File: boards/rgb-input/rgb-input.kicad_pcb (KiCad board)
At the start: 2 copper layers, 184.5 x 137 mm, 181 parts, among them J1 Conn_01x02, J13 I2C, J14 Conn_01x04, J2 Conn_01x02, J20 Conn_01x04, J21 Conn_01x02, J22 Conn_01x02, J23 Conn_01x02, J24 Conn_01x02, J25 Conn_01x02, J26 Conn_01x04, J27 Conn_01x04, J28 Conn_01x02, J29 Conn_01x02, J3 Conn_01x02, J30 Conn_01x04, J31 Conn_01x04, J32 Conn_01x04, J33 Conn_01x04, J34 Conn_01x04, J35 Conn_01x04, J36 Conn_01x04, J37 Conn_01x04, J38 Conn_01x04, J39 Conn_01x04, J4 Conn_01x02, J40 Conn_01x04, J41 Conn_01x04, J5 Conn_01x02, J6 Conn_01x02, J7 Conn_01x02, J8 Conn_01x02, J9 Conn_01x02, U1 ESP32-DEVKITC, U13 MCP1502, U15 MCP3425A0T-ECH, U2 MCP3208, U3 R-78K5.0-1.0, U5 TLC5947DAP, U6 TLC5947DAP

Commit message: figured out most of the components, working on placement
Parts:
- removed J1, J2, J21, J22, J23, J24, J25, J28, J29, J3, J4, J5, J6, J7, J8, J9: Conn_01x02, Connector_JST:JST_PH_B2B-PH-K_1x02_P2.00mm_Vertical
- removed J14, J20, J26, J27, J30, J31, J32, J33, J34, J35, J36, J37, J38, J39, J40, J41: Conn_01x04, Connector_JST:JST_PH_B4B-PH-K_1x04_P2.00mm_Vertical
- added ADC0: ~, Connector_JST:JST_PH_B3B-PH-K_1x03_P2.00mm_Vertical, F.Cu at (63.2, 18.2)
- added ADC1: ~, Connector_JST:JST_PH_B3B-PH-K_1x03_P2.00mm_Vertical, F.Cu at (63.2, 25.3)
- added ADC2: ~, Connector_JST:JST_PH_B3B-PH-K_1x03_P2.00mm_Vertical, F.Cu at (63.2, 32.9)
- added ADC3: ~, Connector_JST:JST_PH_B3B-PH-K_1x03_P2.00mm_Vertical, F.Cu at (63.2, 40.5)
- added ADC4: ~, Connector_JST:JST_PH_B3B-PH-K_1x03_P2.00mm_Vertical, F.Cu at (63.2, 48.1)
- added ADC5: ~, Connector_JST:JST_PH_B3B-PH-K_1x03_P2.00mm_Vertical, F.Cu at (63.2, 55.7)
- added ADC6: ~, Connector_JST:JST_PH_B3B-PH-K_1x03_P2.00mm_Vertical, F.Cu at (63.2, 63.4)
- added ADC7: ~, Connector_JST:JST_PH_B3B-PH-K_1x03_P2.00mm_Vertical, F.Cu at (63.2, 71.0)
- added INPUT0: ~, Connector_JST:JST_PH_B2B-PH-K_1x02_P2.00mm_Vertical, F.Cu at (133.8, 18.2)
- added INPUT1: ~, Connector_JST:JST_PH_B2B-PH-K_1x02_P2.00mm_Vertical, F.Cu at (133.8, 25.8)
- added INPUT10: ~, Connector_JST:JST_PH_B2B-PH-K_1x02_P2.00mm_Vertical, F.Cu at (133.8, 94.4)
- added INPUT11: ~, Connector_JST:JST_PH_B2B-PH-K_1x02_P2.00mm_Vertical, F.Cu at (133.8, 102.0)
- added INPUT12: ~, Connector_JST:JST_PH_B2B-PH-K_1x02_P2.00mm_Vertical, F.Cu at (133.8, 109.6)
- added INPUT13: ~, Connector_JST:JST_PH_B2B-PH-K_1x02_P2.00mm_Vertical, F.Cu at (133.8, 117.2)
- added INPUT14: ~, Connector_JST:JST_PH_B2B-PH-K_1x02_P2.00mm_Vertical, F.Cu at (133.8, 124.9)
- added INPUT15: ~, Connector_JST:JST_PH_B2B-PH-K_1x02_P2.00mm_Vertical, F.Cu at (133.8, 132.5)
- added INPUT2: ~, Connector_JST:JST_PH_B2B-PH-K_1x02_P2.00mm_Vertical, F.Cu at (133.8, 33.4)
- added INPUT3: ~, Connector_JST:JST_PH_B2B-PH-K_1x02_P2.00mm_Vertical, F.Cu at (133.8, 41.0)
- added INPUT4: ~, Connector_JST:JST_PH_B2B-PH-K_1x02_P2.00mm_Vertical, F.Cu at (133.8, 48.7)
- added INPUT5: ~, Connector_JST:JST_PH_B2B-PH-K_1x02_P2.00mm_Vertical, F.Cu at (133.8, 56.3)
- added INPUT6: ~, Connector_JST:JST_PH_B2B-PH-K_1x02_P2.00mm_Vertical, F.Cu at (133.8, 63.9)
- added INPUT7: ~, Connector_JST:JST_PH_B2B-PH-K_1x02_P2.00mm_Vertical, F.Cu at (133.8, 71.5)
- added INPUT8: ~, Connector_JST:JST_PH_B2B-PH-K_1x02_P2.00mm_Vertical, F.Cu at (133.8, 79.1)
- added INPUT9: ~, Connector_JST:JST_PH_B2B-PH-K_1x02_P2.00mm_Vertical, F.Cu at (133.8, 86.8)
- added J42: INPUTS, Connector_IDC:IDC-Header_2x10_P2.54mm_Vertical, F.Cu at (4.77, 100.7)
- added J46: RGB, Connector_IDC:IDC-Header_2x25_P2.54mm_Vertical, F.Cu at (177.7, 105.8)
- added RGB0: ~, Connector_JST:JST_PH_B4B-PH-K_1x04_P2.00mm_Vertical, F.Cu at (151.6, 18.2)
- added RGB1: ~, Connector_JST:JST_PH_B4B-PH-K_1x04_P2.00mm_Vertical, F.Cu at (151.6, 25.8)
- added RGB10: ~, Connector_JST:JST_PH_B4B-PH-K_1x04_P2.00mm_Vertical, F.Cu at (151.6, 94.4)
- added RGB11: ~, Connector_JST:JST_PH_B4B-PH-K_1x04_P2.00mm_Vertical, F.Cu at (151.6, 102.0)
- added RGB12: ~, Connector_JST:JST_PH_B4B-PH-K_1x04_P2.00mm_Vertical, F.Cu at (151.6, 109.6)
- added RGB13: ~, Connector_JST:JST_PH_B4B-PH-K_1x04_P2.00mm_Vertical, F.Cu at (151.6, 117.2)
- added RGB14: ~, Connector_JST:JST_PH_B4B-PH-K_1x04_P2.00mm_Vertical, F.Cu at (151.6, 124.9)
- added RGB15: ~, Connector_JST:JST_PH_B4B-PH-K_1x04_P2.00mm_Vertical, F.Cu at (151.6, 132.5)
- added RGB2: ~, Connector_JST:JST_PH_B4B-PH-K_1x04_P2.00mm_Vertical, F.Cu at (151.6, 33.4)
- added RGB3: ~, Connector_JST:JST_PH_B4B-PH-K_1x04_P2.00mm_Vertical, F.Cu at (151.6, 41.0)
- added RGB4: ~, Connector_JST:JST_PH_B4B-PH-K_1x04_P2.00mm_Vertical, F.Cu at (151.6, 48.7)
- added RGB5: ~, Connector_JST:JST_PH_B4B-PH-K_1x04_P2.00mm_Vertical, F.Cu at (151.6, 56.3)
- added RGB6: ~, Connector_JST:JST_PH_B4B-PH-K_1x04_P2.00mm_Vertical, F.Cu at (151.6, 63.9)
- added RGB7: ~, Connector_JST:JST_PH_B4B-PH-K_1x04_P2.00mm_Vertical, F.Cu at (151.6, 71.5)
- added RGB8: ~, Connector_JST:JST_PH_B4B-PH-K_1x04_P2.00mm_Vertical, F.Cu at (151.6, 79.1)
- added RGB9: ~, Connector_JST:JST_PH_B4B-PH-K_1x04_P2.00mm_Vertical, F.Cu at (151.6, 86.8)
- moved U6 217.7 mm to (175.7, 122.3)
- moved U5 206.8 mm to (177.0, 28.3)
- moved H2 185.9 mm to (180.8, 133.8)
- moved C3 107.2 mm to (125.8, 185.9)
- moved D2 107.2 mm to (125.8, 188.4)
- moved R1 107.2 mm to (122.0, 188.4)
- moved R2 107.2 mm to (122.0, 185.9)
- moved C17 81.4 mm to (115.1, 168.1)
- moved D12 81.4 mm to (111.8, 194.8)
- moved D13 81.4 mm to (100.9, 194.8)
- moved R22 81.4 mm to (116.0, 179.6)
- moved R25 81.4 mm to (126.9, 179.6)
- moved R26 81.4 mm to (105.2, 179.6)
- moved R4 81.4 mm to (94.3, 178.1)
- moved R44 81.4 mm to (79.9, 178.1)
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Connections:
- net /ADC Input/INPUT renamed /ADC Input0/INPUT
- net /Input Switch0/INPUT renamed /INPUT0
- net /Input Switch1/INPUT renamed /INPUT1
- net /Input Switch10/INPUT renamed /INPUT10
- net /Input Switch11/INPUT renamed /INPUT11
- net /Input Switch12/INPUT renamed /INPUT12
- net /Input Switch13/INPUT renamed /INPUT13
- net /Input Switch14/INPUT renamed /INPUT14
- net /Input Switch15/INPUT renamed /INPUT15
- net /Input Switch2/INPUT renamed /INPUT2
- net /Input Switch3/INPUT renamed /INPUT3
- net /Input Switch4/INPUT renamed /INPUT4
- net /Input Switch5/INPUT renamed /INPUT5
- net /Input Switch6/INPUT renamed /INPUT6
- net /Input Switch7/INPUT renamed /INPUT7
- net /Input Switch8/INPUT renamed /INPUT8
- net /Input Switch9/INPUT renamed /INPUT9
- U5 pad 10: /LEDS/LED Driver1/OUT5 -> /LEDS/BLUE9
- U5 pad 11: /LEDS/LED Driver1/OUT6 -> /LEDS/RED10
- U5 pad 12: /LEDS/LED Driver1/OUT7 -> /LEDS/GREEN10
- U5 pad 13: /LEDS/LED Driver1/OUT8 -> /LEDS/BLUE10
- U5 pad 14: /LEDS/LED Driver1/OUT9 -> /LEDS/RED11
- U5 pad 15: /LEDS/LED Driver1/OUT10 -> /LEDS/GREEN11
- U5 pad 16: /LEDS/LED Driver1/OUT11 -> /LEDS/BLUE11
- U5 pad 17: /LEDS/LED Driver1/OUT12 -> /LEDS/RED12
- U5 pad 18: /LEDS/LED Driver1/OUT13 -> /LEDS/GREEN12
- U5 pad 19: /LEDS/LED Driver1/OUT14 -> /LEDS/BLUE12
- U5 pad 20: /LEDS/LED Driver1/OUT15 -> /LEDS/RED13
- U5 pad 21: /LEDS/LED Driver1/OUT16 -> /LEDS/GREEN13
- U5 pad 22: /LEDS/LED Driver1/OUT17 -> /LEDS/BLUE13
- U5 pad 23: /LEDS/LED Driver1/OUT18 -> /LEDS/RED14
- U5 pad 24: /LEDS/LED Driver1/OUT19 -> /LEDS/GREEN14
- U5 pad 25: /LEDS/LED Driver1/OUT20 -> /LEDS/BLUE14
- U5 pad 26: /LEDS/LED Driver1/OUT21 -> /LEDS/RED15
- U5 pad 27: /LEDS/LED Driver1/OUT22 -> /LEDS/GREEN15
- U5 pad 28: /LEDS/LED Driver1/OUT23 -> /LEDS/BLUE15
- U5 pad 5: /LEDS/LED Driver1/OUT0 -> /LEDS/RED8
- U5 pad 6: /LEDS/LED Driver1/OUT1 -> /LEDS/GREEN8
- U5 pad 7: /LEDS/LED Driver1/OUT2 -> /LEDS/BLUE8
- U5 pad 8: /LEDS/LED Driver1/OUT3 -> /LEDS/RED9
- U5 pad 9: /LEDS/LED Driver1/OUT4 -> /LEDS/GREEN9
- U6 pad 10: /LEDS/LED Driver/OUT5 -> /LEDS/BLUE1
- U6 pad 11: /LEDS/LED Driver/OUT6 -> /LEDS/RED2
- U6 pad 12: /LEDS/LED Driver/OUT7 -> /LEDS/GREEN2
- U6 pad 13: /LEDS/LED Driver/OUT8 -> /LEDS/BLUE2
- U6 pad 14: /LEDS/LED Driver/OUT9 -> /LEDS/RED3
- U6 pad 15: /LEDS/LED Driver/OUT10 -> /LEDS/GREEN3
- U6 pad 16: /LEDS/LED Driver/OUT11 -> /LEDS/BLUE3
- U6 pad 17: /LEDS/LED Driver/OUT12 -> /LEDS/RED4
- U6 pad 18: /LEDS/LED Driver/OUT13 -> /LEDS/GREEN4
- U6 pad 19: /LEDS/LED Driver/OUT14 -> /LEDS/BLUE4
- U6 pad 20: /LEDS/LED Driver/OUT15 -> /LEDS/RED5
- U6 pad 21: /LEDS/LED Driver/OUT16 -> /LEDS/GREEN5
- U6 pad 22: /LEDS/LED Driver/OUT17 -> /LEDS/BLUE5
- U6 pad 23: /LEDS/LED Driver/OUT18 -> /LEDS/RED6
- U6 pad 24: /LEDS/LED Driver/OUT19 -> /LEDS/GREEN6
- U6 pad 25: /LEDS/LED Driver/OUT20 -> /LEDS/BLUE6
- U6 pad 26: /LEDS/LED Driver/OUT21 -> /LEDS/RED7
- U6 pad 27: /LEDS/LED Driver/OUT22 -> /LEDS/GREEN7
- U6 pad 28: /LEDS/LED Driver/OUT23 -> /LEDS/BLUE7
- U6 pad 5: /LEDS/LED Driver/OUT0 -> /LEDS/RED0
- U6 pad 6: /LEDS/LED Driver/OUT1 -> /LEDS/GREEN0
- U6 pad 7: /LEDS/LED Driver/OUT2 -> /LEDS/BLUE0
- U6 pad 8: /LEDS/LED Driver/OUT3 -> /LEDS/RED1
- U6 pad 9: /LEDS/LED Driver/OUT4 -> /LEDS/GREEN1
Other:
- outline, holes or cut-outs redrawn
- board text removed: "CAN"
- board text removed: "LFAN"
- board text removed: "RFAN"
- board text removed: "RX"
- board text removed: "TX"

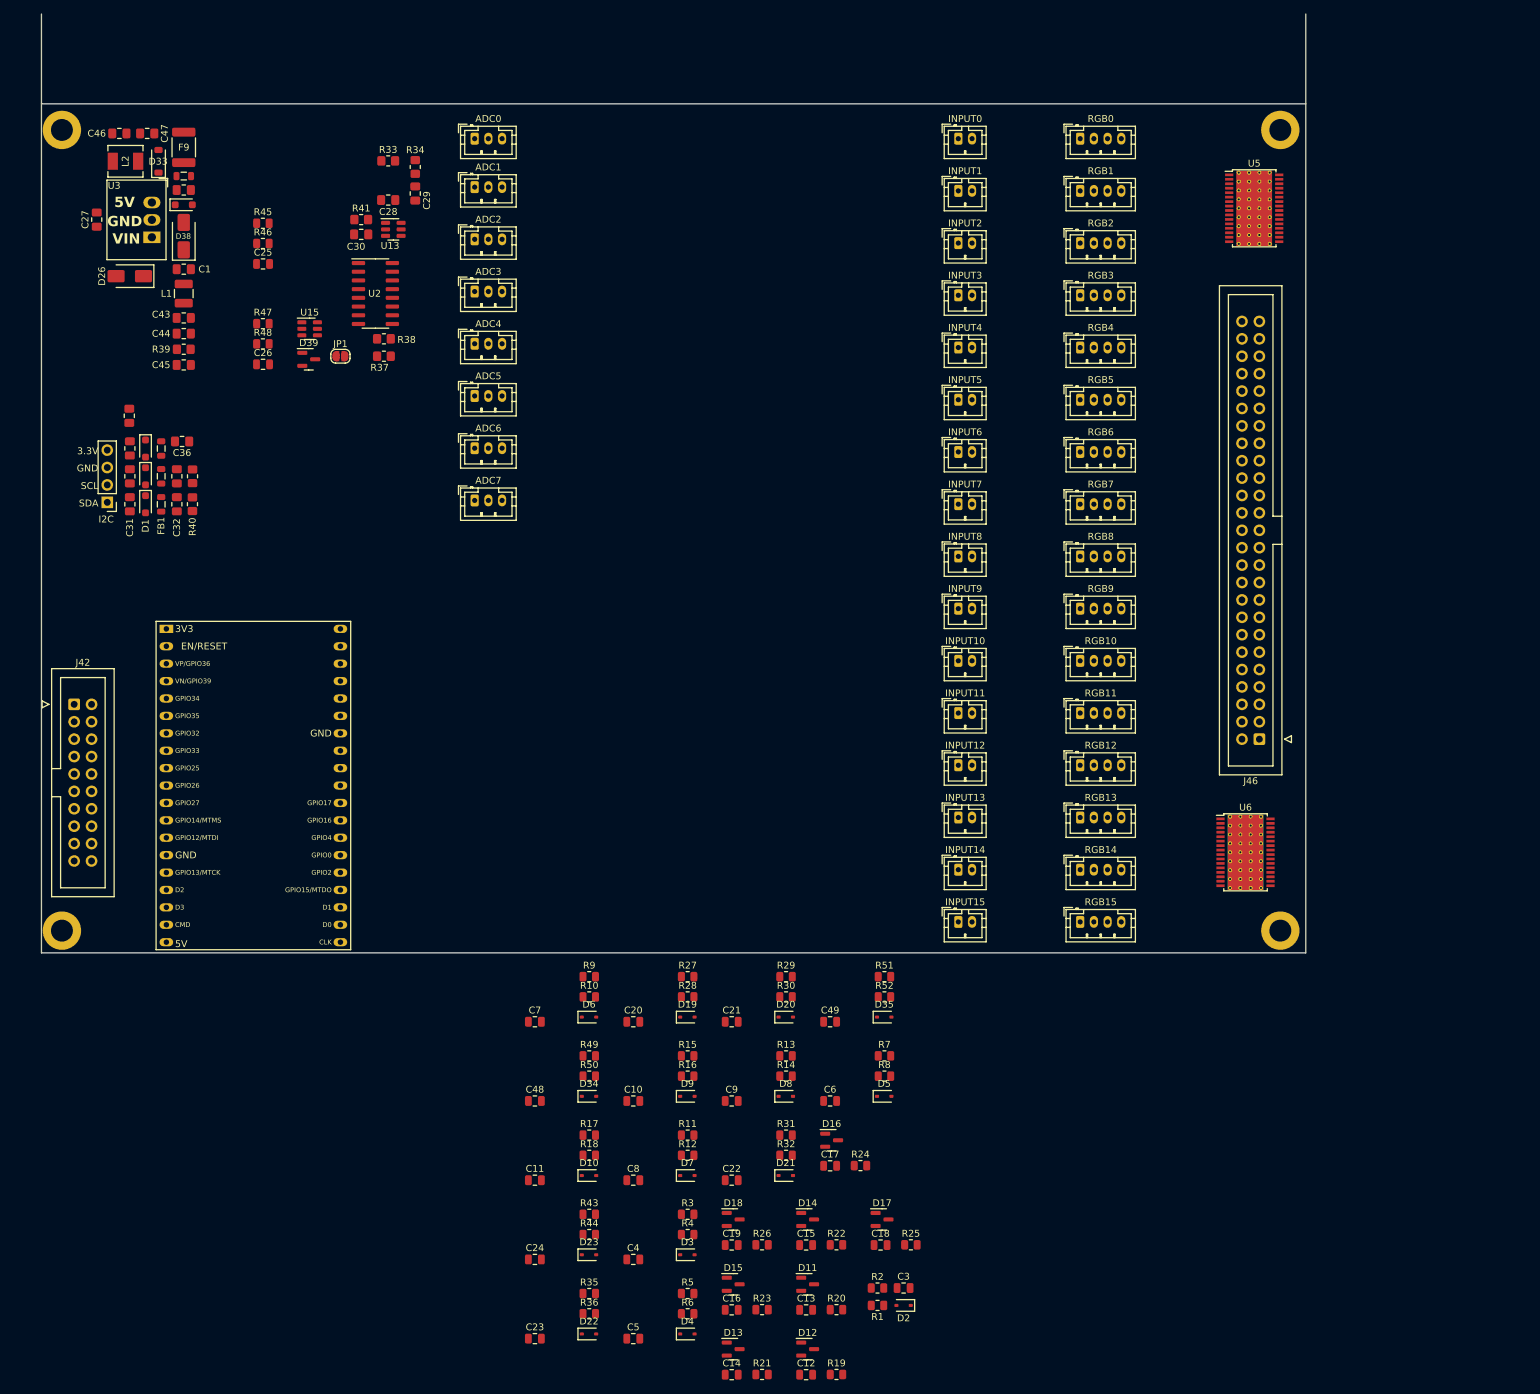
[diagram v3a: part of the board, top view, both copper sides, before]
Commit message: more layout checks on the input board
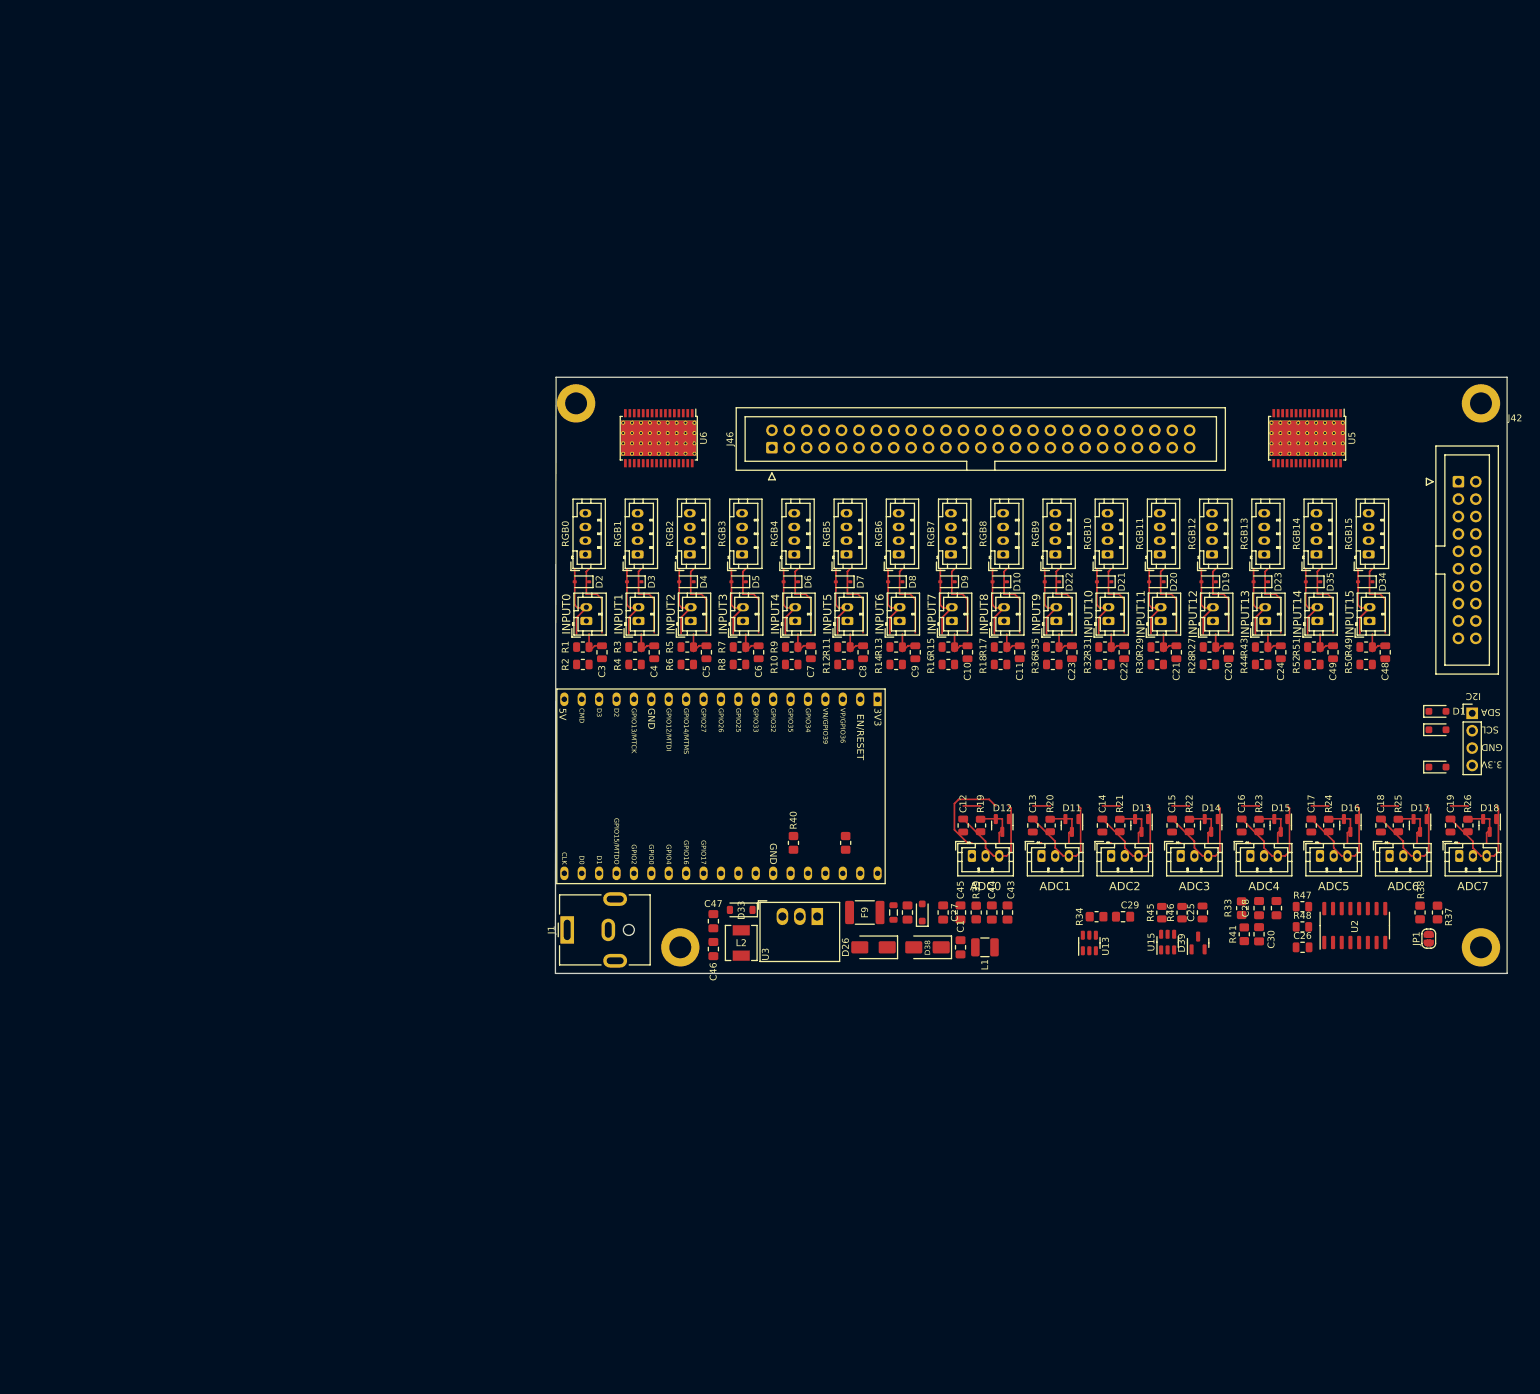
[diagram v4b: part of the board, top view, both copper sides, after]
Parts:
- removed C31, C32, C33, C34: 33pF, Capacitor_SMD:C_0805_2012Metric_Pad1.18x1.45mm_HandSolder
- removed C35, C36: 10uF, Capacitor_SMD:C_0805_2012Metric_Pad1.18x1.45mm_HandSolder
- removed FB1, FB2, FB3: GZ2012D601TF, Inductor_SMD:L_0805_2012Metric
- added J1: Barrel_Jack, Connector_BarrelJack:BarrelJack_CUI_PJ-063AH_Horizontal, F.Cu at (76.7, 133.7)
- moved J42 204.6 mm to (206.8, 68.2)
- moved J13 201.6 mm to (208.8, 102.0), turned to 0 degrees
- moved D28 194.2 mm to (203.7, 109.9), turned to 0 degrees
- moved D27 192.1 mm to (203.7, 104.4), turned to 0 degrees
- moved D1 190.9 mm to (203.7, 101.8), turned to 0 degrees
- moved C37 182.2 mm to (180.2, 130.5)
- moved JP1 180.1 mm to (202.4, 134.9), turned to 90 degrees
- moved R48 173.9 mm to (184.0, 133.2)
- moved C26 173.9 mm to (184.0, 136.2)
- moved R47 173.9 mm to (184.0, 130.3)
- moved R37 173.9 mm to (203.7, 131.1), turned to -90 degrees
- moved R38 172.8 mm to (201.2, 131.1), turned to 90 degrees
- moved U2 170.1 mm to (191.7, 133.0), turned to 90 degrees
- moved C25 166.6 mm to (169.4, 131.1), turned to 90 degrees
- moved C30 166.1 mm to (177.7, 134.3), turned to 90 degrees
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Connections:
- ADC0 pad 1: Net-(ADC0-Pin_1) -> +3V3
- ADC0 pad 2: +3V3 -> GNDD
- ADC0 pad 3: GNDD -> Net-(ADC0-Pin_3)
- ADC1 pad 1: Net-(ADC1-Pin_1) -> +3V3
- ADC1 pad 2: +3V3 -> GNDD
- ADC1 pad 3: GNDD -> Net-(ADC1-Pin_3)
- ADC2 pad 1: Net-(ADC2-Pin_1) -> +3V3
- ADC2 pad 2: +3V3 -> GNDD
- ADC2 pad 3: GNDD -> Net-(ADC2-Pin_3)
- ADC3 pad 1: Net-(ADC3-Pin_1) -> +3V3
- ADC3 pad 2: +3V3 -> GNDD
- ADC3 pad 3: GNDD -> Net-(ADC3-Pin_3)
- ADC4 pad 1: Net-(ADC4-Pin_1) -> +3V3
- ADC4 pad 2: +3V3 -> GNDD
- ADC4 pad 3: GNDD -> Net-(ADC4-Pin_3)
- ADC5 pad 1: Net-(ADC5-Pin_1) -> +3V3
- ADC5 pad 2: +3V3 -> GNDD
- ADC5 pad 3: GNDD -> Net-(ADC5-Pin_3)
- ADC6 pad 1: Net-(ADC6-Pin_1) -> +3V3
- ADC6 pad 2: +3V3 -> GNDD
- ADC6 pad 3: GNDD -> Net-(ADC6-Pin_3)
- ADC7 pad 1: Net-(ADC7-Pin_1) -> +3V3
- ADC7 pad 2: +3V3 -> GNDD
- ADC7 pad 3: GNDD -> Net-(ADC7-Pin_3)
- D1 pad 2: Net-(D1-A2) -> SDA
- D11 pad 3: Net-(ADC1-Pin_1) -> Net-(ADC1-Pin_3)
- D12 pad 3: Net-(ADC0-Pin_1) -> Net-(ADC0-Pin_3)
- D13 pad 3: Net-(ADC2-Pin_1) -> Net-(ADC2-Pin_3)
- D14 pad 3: Net-(ADC3-Pin_1) -> Net-(ADC3-Pin_3)
- D15 pad 3: Net-(ADC4-Pin_1) -> Net-(ADC4-Pin_3)
- D16 pad 3: Net-(ADC5-Pin_1) -> Net-(ADC5-Pin_3)
- D17 pad 3: Net-(ADC6-Pin_1) -> Net-(ADC6-Pin_3)
- D18 pad 3: Net-(ADC7-Pin_1) -> Net-(ADC7-Pin_3)
- D27 pad 2: Net-(D27-A2) -> SCL
- D28 pad 2: Net-(D28-A2) -> +3.3V
- J13 pad 1: Net-(D1-A2) -> SDA
- J13 pad 2: Net-(D27-A2) -> SCL
- J13 pad 4: Net-(D28-A2) -> +3.3V
- R19 pad 1: Net-(ADC0-Pin_1) -> Net-(ADC0-Pin_3)
- R20 pad 1: Net-(ADC1-Pin_1) -> Net-(ADC1-Pin_3)
- R21 pad 1: Net-(ADC2-Pin_1) -> Net-(ADC2-Pin_3)
- R22 pad 1: Net-(ADC3-Pin_1) -> Net-(ADC3-Pin_3)
- R23 pad 1: Net-(ADC4-Pin_1) -> Net-(ADC4-Pin_3)
- R24 pad 1: Net-(ADC5-Pin_1) -> Net-(ADC5-Pin_3)
- R25 pad 1: Net-(ADC6-Pin_1) -> Net-(ADC6-Pin_3)
- R26 pad 1: Net-(ADC7-Pin_1) -> Net-(ADC7-Pin_3)
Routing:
- net GNDD: track 0.00 -> 330.8 mm
- net Net-(D8-A2): track 0.00 -> 11.6 mm
- net Net-(D5-A2): track 0.00 -> 11.6 mm
- net Net-(D35-A2): track 0.00 -> 11.6 mm
- net Net-(D34-A2): track 0.00 -> 11.6 mm
- net Net-(D22-A2): track 0.00 -> 11.6 mm
- net Net-(D21-A2): track 0.00 -> 11.6 mm
- net Net-(D20-A2): track 0.00 -> 11.6 mm
- net Net-(D2-A2): track 0.00 -> 11.6 mm
- net Net-(D10-A2): track 0.00 -> 11.6 mm
- net Net-(D7-A2): track 0.00 -> 11.6 mm
- net Net-(D4-A2): track 0.00 -> 11.6 mm
- net Net-(D9-A2): track 0.00 -> 11.6 mm
- net Net-(D23-A2): track 0.00 -> 11.6 mm
- net Net-(D3-A2): track 0.00 -> 11.6 mm
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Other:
- board size 184.5 x 137 mm -> 138.9 x 87 mm
- board text removed: "5V"
- board text removed: "VIN"
